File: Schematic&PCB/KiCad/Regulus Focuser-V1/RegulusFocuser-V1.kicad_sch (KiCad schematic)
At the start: 44 parts, among them J1 USB_A, J2 Display&Encoder, J3 Serial1, J4 R-Connect, J5 MotorPower, J6 MotorConnector, J7 5V-Ext, J8 LimiterSW, J9 ResetSW, U1 FT232RL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

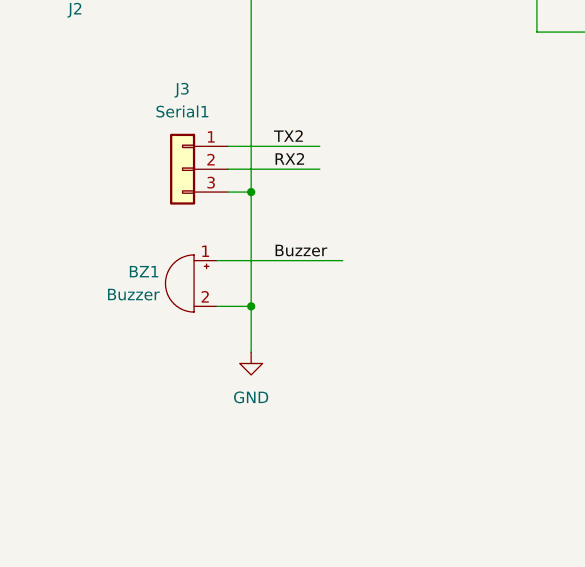
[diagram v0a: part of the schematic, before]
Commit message: Added backlash aid in firmware
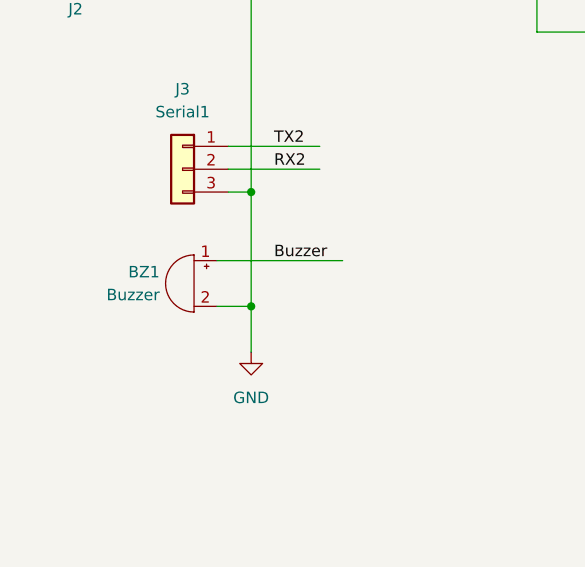
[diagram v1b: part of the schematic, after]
